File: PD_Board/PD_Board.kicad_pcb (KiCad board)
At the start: 2 copper layers, 14 parts

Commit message: started schematic layout
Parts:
- moved T10 57.6 mm to (118.5, 112.0), turned to -90 degrees
- moved H3 50.5 mm to (131.0, 133.5)
- moved T6 39.8 mm to (159.0, 73.0)
- moved H4 39.4 mm to (210.0, 113.0)
- moved T9 36.1 mm to (159.0, 93.0)
- moved T7 34.1 mm to (159.0, 85.0)
- moved T8 34.1 mm to (159.0, 90.5)
- moved T3 33.7 mm to (193.0, 107.5)
- moved H2 33.1 mm to (209.5, 134.0)
- moved H1 32.4 mm to (130.5, 112.5)
- moved T5 31.1 mm to (159.0, 79.0)
- moved T1 30.8 mm to (151.0, 87.5), turned to 180 degrees
- moved T4 22.7 mm to (140.0, 93.0)
- moved T2 20.3 mm to (229.5, 113.5), turned to -90 degrees
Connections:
- T1 pad 1: unconnected-(T1-Pad1) -> Net-(T1-Pad1)
- T1 pad 2: unconnected-(T1-Pad2) -> Net-(T1-Pad2)
- T1 pad 3: unconnected-(T1-Pad3) -> Net-(T3--)
- T1 pad 4: unconnected-(T1-Pad4) -> Net-(T3-+)
- T10 pad 1: unconnected-(T10-Pad1) -> Net-(T10-Pad1)
- T10 pad 2: unconnected-(T10-Pad2) -> Net-(T3--)
- T10 pad 3: unconnected-(T10-Pad3) -> Net-(T3-+)
- T2 pad 1: unconnected-(T2-Pad1) -> Net-(T2-Pad1)
- T2 pad 2: unconnected-(T2-Pad2) -> Net-(T3--)
- T2 pad 3: unconnected-(T2-Pad3) -> Net-(T3-+)
- T3 pad 1: unconnected-(T3-+-Pad1) -> Net-(T3-+)
- T3 pad 2: unconnected-(T3---Pad2) -> Net-(T3--)
- T4 pad 1: unconnected-(T4-Pad1) -> Net-(T4-Pad1)
- T4 pad 2: unconnected-(T4-Pad2) -> Net-(T3--)
- T4 pad 3: unconnected-(T4-Pad3) -> Net-(T3-+)
- T5 pad 1: unconnected-(T5-Pad1) -> Net-(T10-Pad1)
- T6 pad 1: unconnected-(T6-Pad1) -> Net-(T4-Pad1)
- T7 pad 1: unconnected-(T7-Pad1) -> Net-(T2-Pad1)
- T8 pad 1: unconnected-(T8-Pad1) -> Net-(T1-Pad2)
- T9 pad 1: unconnected-(T9-Pad1) -> Net-(T1-Pad1)
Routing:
- added copper zone on F.Cu, net Net-(T3-+)
- added copper zone on F.Cu, net Net-(T3--)
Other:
- board outline added: 140 x 42 mm

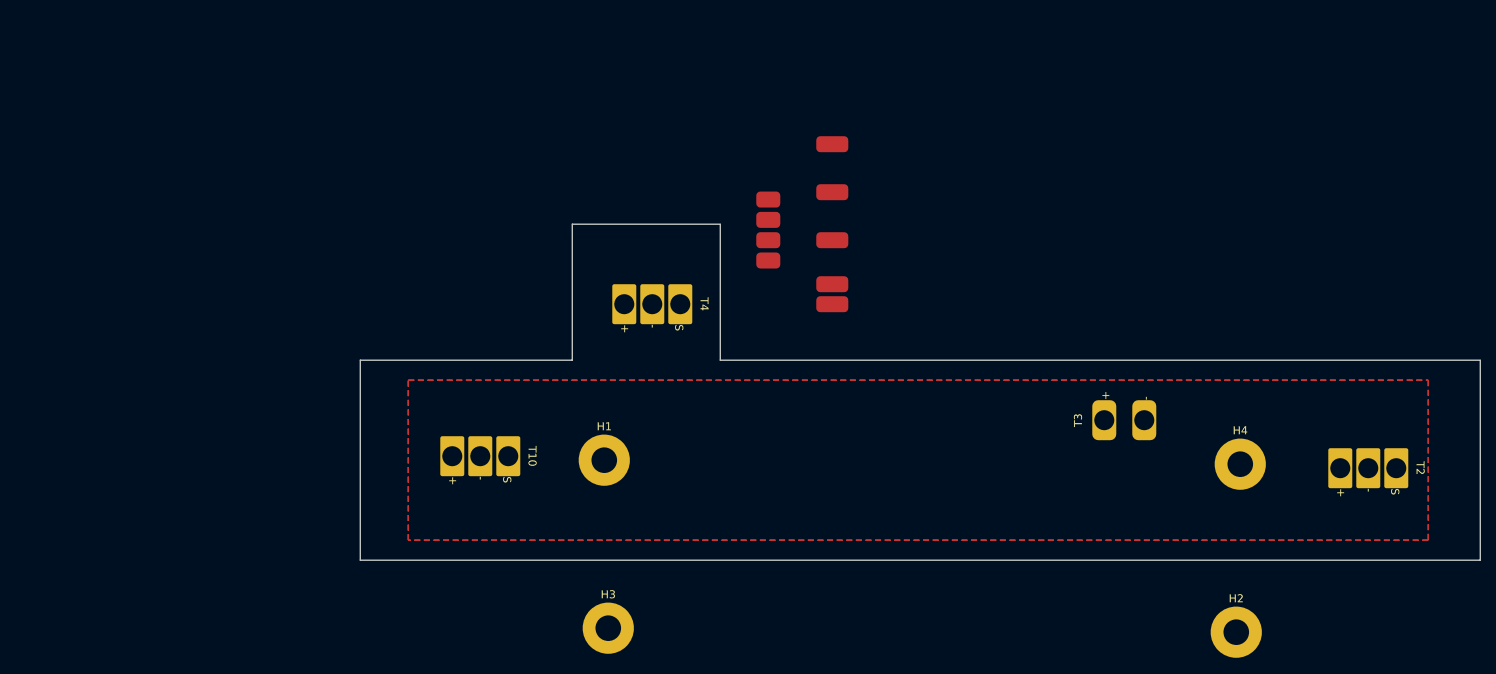
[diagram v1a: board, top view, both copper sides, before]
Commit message: Removed 2 screw mounts
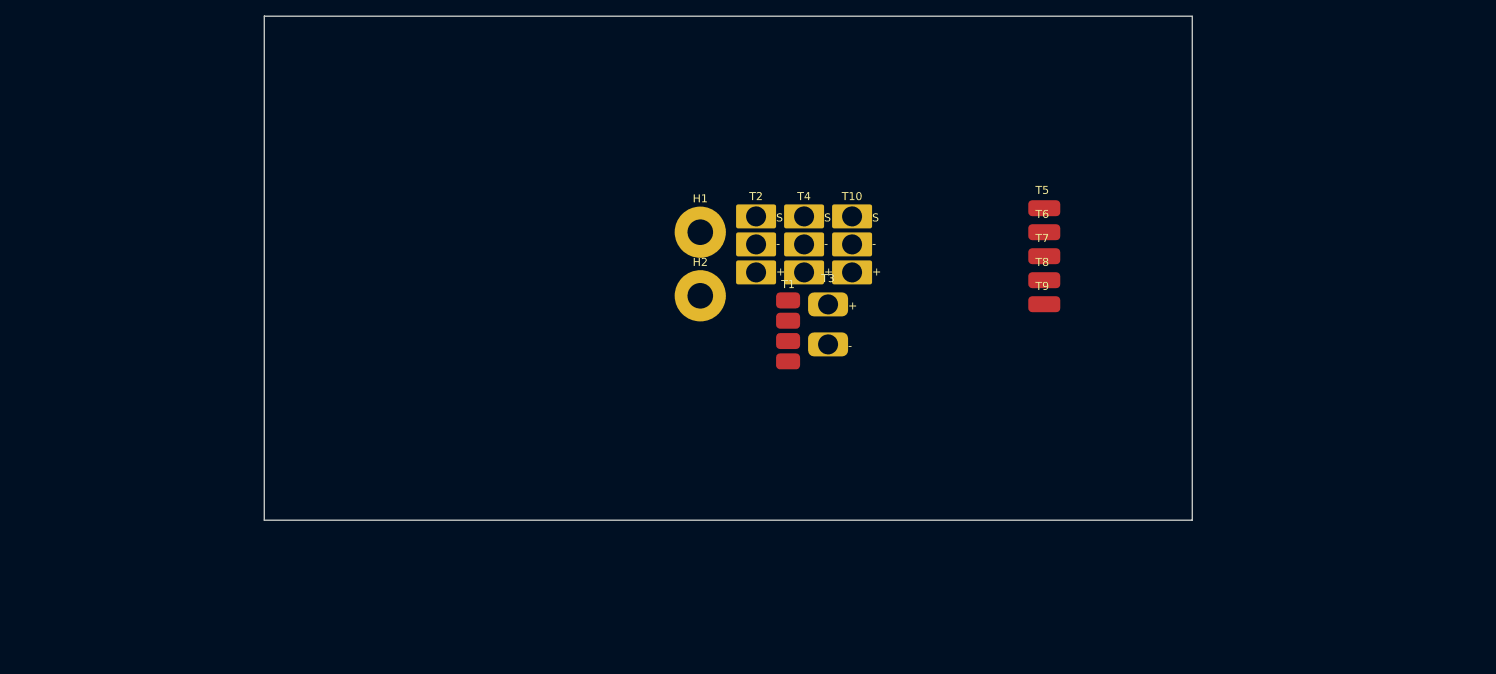
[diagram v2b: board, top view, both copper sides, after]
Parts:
- removed H3, H4: MountingHole, MountingHole:MountingHole_3.2mm_M3_Pad
- moved T2 86.0 mm to (149.5, 82.0), turned to 0 degrees
- moved H2 79.1 mm to (142.5, 92.0)
- moved T10 52.4 mm to (161.5, 82.0), turned to 0 degrees
- moved T3 37.4 mm to (158.5, 93.0), turned to 0 degrees
- moved H1 30.9 mm to (142.5, 84.0)
- moved T6 28.7 mm to (185.5, 84.0)
- moved T5 26.6 mm to (185.5, 81.0)
- moved T7 26.6 mm to (185.5, 87.0)
- moved T8 26.5 mm to (185.5, 90.0)
- moved T9 26.5 mm to (185.5, 93.0)
- moved T4 19.0 mm to (155.5, 82.0), turned to 0 degrees
- moved T1 5.57 mm to (153.5, 92.5), turned to 0 degrees
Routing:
- removed copper zone on F.Cu, net Net-(T3-+)
- removed copper zone on F.Cu, net Net-(T3--)
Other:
- board size 140 x 42 mm -> 116 x 63 mm

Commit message: womp womp
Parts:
- moved T7 83.6 mm to (104.5, 107.5), turned to 180 degrees
- moved T5 58.9 mm to (130.2, 101.5)
- moved T2 55.5 mm to (104.5, 114.5)
- moved T8 54.6 mm to (141.5, 122.2), turned to 180 degrees
- moved T9 45.8 mm to (150.2, 122.2), turned to 180 degrees
- moved T4 44.6 mm to (185.8, 114.8)
- moved H2 42.5 mm to (176.5, 117.5)
- moved H1 40.3 mm to (114.0, 112.5)
- moved T1 29.2 mm to (159.8, 121.0), turned to 90 degrees
- moved T6 27.8 mm to (185.8, 111.8), turned to 180 degrees
- moved T10 25.7 mm to (141.0, 66.5)
- moved T3 23.5 mm to (177.8, 106.5), turned to 90 degrees
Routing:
- net Net-(T1-Pad2): track 0.00 -> 25.1 mm
- net Net-(T1-Pad1): track 0.00 -> 10.0 mm
- net Net-(T2-Pad1): track 0.00 -> 7.00 mm
- net Net-(T4-Pad1): track 0.00 -> 3.00 mm
- net Net-(T3--): vias 0 -> 1
- added copper zone on F.Cu, net Net-(T3-+)
- added copper zone on B.Cu, net Net-(T3--)
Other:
- board size 116 x 63 mm -> 90 x 25 mm

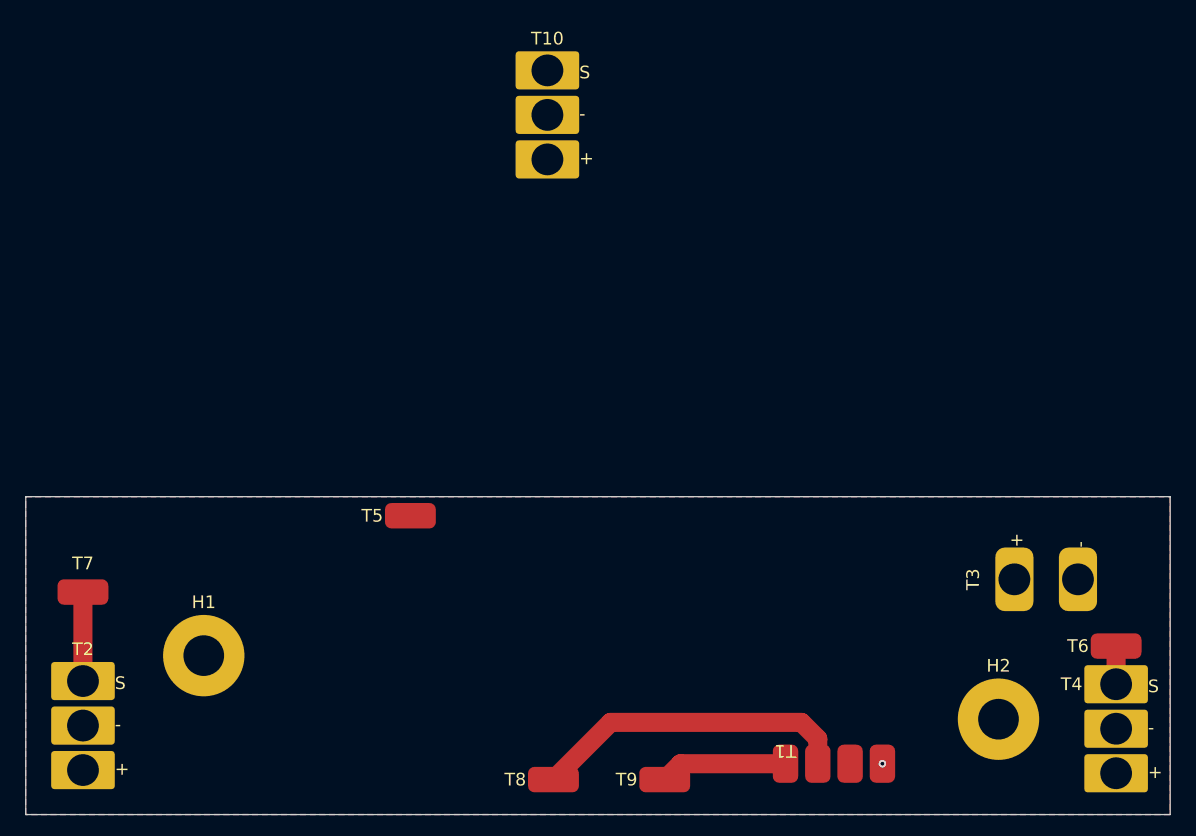
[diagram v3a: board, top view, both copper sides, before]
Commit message: Added wing onto pcb for weapon ese
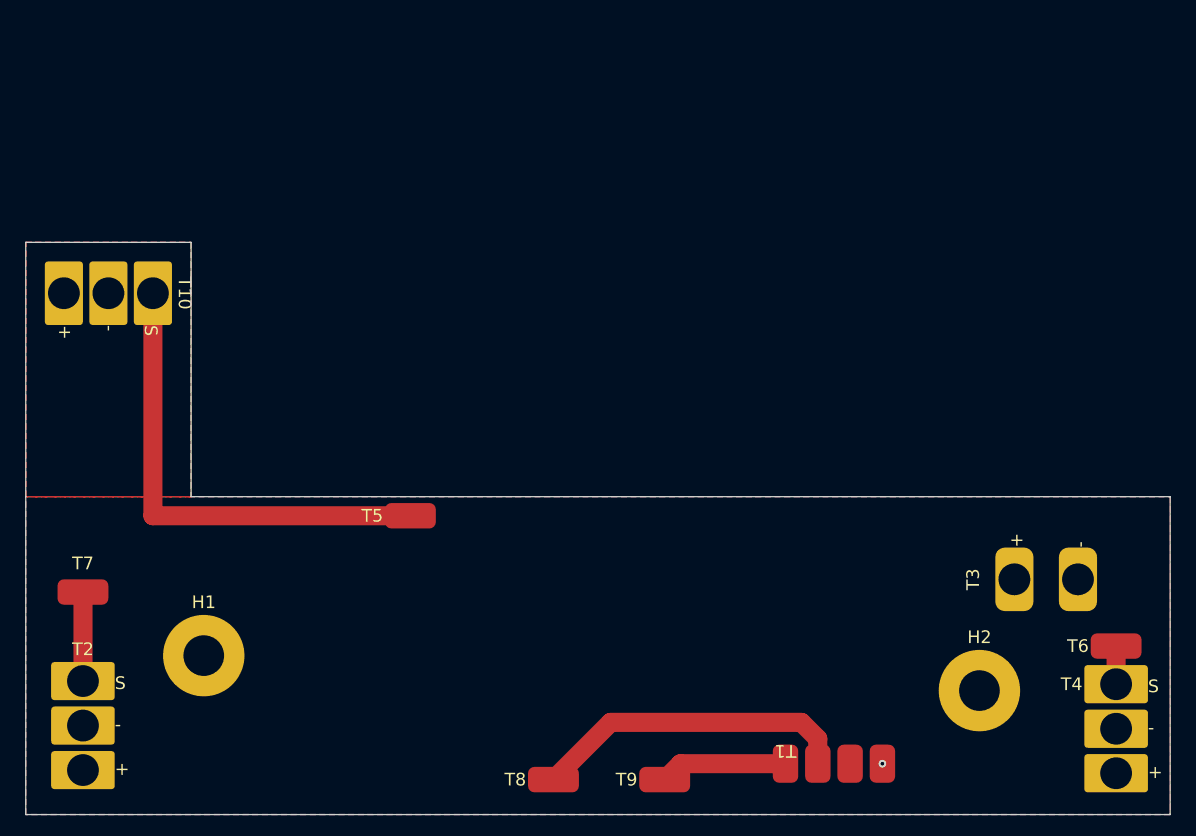
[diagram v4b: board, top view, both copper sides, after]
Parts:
- moved T10 35.6 mm to (110.0, 84.0), turned to -90 degrees
- moved H2 2.70 mm to (175.0, 115.2)
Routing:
- net Net-(T10-Pad1): track 0.00 -> 37.8 mm
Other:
- board size 90 x 25 mm -> 90 x 45 mm
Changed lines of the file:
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@@
 	(footprint "MountingHole:MountingHole_3.2mm_M3_Pad"
 		(layer "F.Cu")
-		(at 176.5 117.5)
+		(at 175 115.25)
 		(descr "Mounting Hole 3.2mm, M3")
 		(tags "mounting hole 3.2mm m3")
@@
 	(footprint "Connectors:MR30"
 		(layer "F.Cu")
-		(at 141.025 66.475)
+		(at 110 84 -90)
 		(property "Reference" "T10"
-			(at 0 -2.5 0)
+			(at 0 -2.5 -90)
 			(unlocked yes)
 			(layer "F.SilkS")
@@
 		)
 		(property "Value" "~"
-			(at 0 11.5 0)
+			(at 0 11.5 -90)
 			(unlocked yes)
 			(layer "F.Fab")
@@
 		)
 		(property "Footprint" "Connectors:MR30"
-			(at 0 0 0)
+			(at 0 0 -90)
 			(unlocked yes)
 			(layer "F.Fab")
@@
 		)
 		(property "Datasheet" ""
-			(at 0 0 0)
+			(at 0 0 -90)
 			(unlocked yes)
 			(layer "F.Fab")
@@
 		)
 		(property "Description" ""
-			(at 0 0 0)
+			(at 0 0 -90)
 			(unlocked yes)
 			(layer "F.Fab")
@@
 		(attr smd)
 		(fp_text user "+"
-			(at 2.5 7.5 0)
+			(at 2.5 7.5 -90)
 			(unlocked yes)
 			(layer "F.SilkS")
@@
 		)
 		(fp_text user "-"
-			(at 2.5 4 0)
+			(at 2.5 4 -90)
 			(unlocked yes)
 			(layer "F.SilkS")
@@
 		)
 		(fp_text user "S"
-			(at 2.5 0.75 0)
+			(at 2.5 0.75 -90)
 			(unlocked yes)
 			(layer "F.SilkS")
@@
 		)
 		(fp_text user "${REFERENCE}"
-			(at 0 10 0)
+			(at 0 10 -90)
 			(unlocked yes)
 			(layer "F.Fab")
@@
 		)
 		(pad "1" thru_hole roundrect
-			(at 0 0)
+			(at 0 0 270)
 			(size 5 3)
 			(drill 2.5)
@@
 		)
 		(pad "2" thru_hole roundrect
-			(at 0 3.5)
+			(at 0 3.5 270)
 			(size 5 3)
 			(drill 2.5)
@@
 		)
 		(pad "3" thru_hole roundrect
-			(at 0 7)
+			(at 0 7 270)
 			(size 5 3)
 			(drill 2.5)
@@
 		)
 	)
-	(gr_rect
+	(gr_line
+		(start 113 80)
+		(end 113 100)
+		(stroke
+			(width 0.05)
+			(type default)
+		)
+		(layer "Edge.Cuts")
+	)
+	(gr_line
+		(start 190 125)
+		(end 100 125)
+		(stroke
+			(width 0.05)
+			(type default)
+		)
+		(layer "Edge.Cuts")
+	)
+	(gr_line
 		(start 100 100)
+		(end 100 80)
+		(stroke
+			(width 0.05)
+			(type default)
+		)
+		(layer "Edge.Cuts")
+	)
+	(gr_line
+		(start 100 125)
+		(end 100 100)
+		(stroke
+			(width 0.05)
+			(type default)
+		)
+		(layer "Edge.Cuts")
+	)
+	(gr_line
+		(start 113 100)
+		(end 190 100)
+		(stroke
+			(width 0.05)
+			(type default)
+		)
+		(layer "Edge.Cuts")
+	)
+	(gr_line
+		(start 190 100)
 		(end 190 125)
 		(stroke
@@
 			(type default)
 		)
-		(fill none)
+		(layer "Edge.Cuts")
+	)
+	(gr_line
+		(start 100 80)
+		(end 113 80)
+		(stroke
+			(width 0.05)
+			(type default)
+		)
 		(layer "Edge.Cuts")
 	)
@@
 		(layer "F.Cu")
 		(net 6)
+	)
+	(segment
+		(start 110 84)
+		(end 110 101.5)
+		(width 1.5)
+		(layer "F.Cu")
+		(net 7)
+	)
+	(segment
+		(start 110 101.5)
+		(end 130.25 101.5)
+		(width 1.5)
+		(layer "F.Cu")
+		(net 7)
+	)
+	(zone
+		(net 1)
+		(net_name "Net-(T3-+)")
+		(layer "F.Cu")
+		(hatch edge 0.5)
+		(priority 2)
+		(connect_pads
+			(clearance 0.5)
+		)
+		(min_thickness 0.25)
+		(filled_areas_thickness no)
+		(fill yes
+			(thermal_gap 0.5)
+			(thermal_bridge_width 0.5)
+		)
+		(polygon
+			(pts
+				(xy 100 100) (xy 100 80) (xy 113 80) (xy 113 100)
+			)
+		)
 	)
 	(zone
@@
 			)
 		)
+	)
+	(zone
+		(net 1)
+		(net_name "Net-(T3-+)")
+		(layer "F.Cu")
+		(hatch edge 0.5)
+		(priority 3)
+		(connect_pads yes
+			(clearance 0.5)
+		)
+		(min_thickness 0.25)
+		(filled_areas_thickness no)
+		(fill yes
+			(thermal_gap 0.5)
+			(thermal_bridge_width 0.5)
+		)
+		(polygon
+			(pts
+				(xy 100 100) (xy 100 80) (xy 113 80) (xy 113 100)
+			)
+		)
+	)
+	(zone
+		(net 3)
+		(net_name "Net-(T3--)")
+		(layer "B.Cu")
+		(hatch edge 0.5)
+		(priority 4)
+		(connect_pads yes
+			(clearance 0.5)
+		)
+		(min_thickness 0.25)
+		(filled_areas_thickness no)
+		(fill yes
+			(thermal_gap 0.5)
+			(thermal_bridge_width 0.5)
+		)
+		(polygon
+			(pts
+				(xy 100 100) (xy 100 80) (xy 113 80) (xy 113 100)
+			)
+		)
